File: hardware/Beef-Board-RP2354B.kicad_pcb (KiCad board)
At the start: 2 copper layers, 84 x 59.2 mm, 81 parts, among them J1 USB-C DEVICE, J10 VAUX OUT, J11 B1 LEGACY, J12 B2 LEGACY, J13 B3 LEGACY, J14 B4 LEGACY, J15 B5 LEGACY, J16 B6 LEGACY, J17 B7 LEGACY, J18 B8 LEGACY, J19 B9 LEGACY, J2 POWER SELECT, J20 B10 LEGACY, J21 B11 LEGACY, J22 USB COMMON, J3 VAUX 5V INPUT, J31 ENCODER 1, J32 ENCODER 2, J33 AE1 0-5V, J34 AE2 0-5V, J4 USB-C AUX POWER, J40 TT RGB, J41 CENTER BAR RGB, J42 UART A 3V3, J43 UART B 3V3, J5 ENC1 A, J6 ENC1 B, J60 RESET HEADER, J61 BOOTSEL HEADER, J7 ENC2 A, J8 ENC2 B, J9 VAUX OUT, Q1 2N7002, Q10 2N7002, Q11 2N7002, Q2 2N7002, Q3 2N7002, Q4 2N7002, Q5 2N7002, Q6 2N7002, Q7 2N7002, Q8 2N7002, Q9 2N7002, U1 RP2354B, U2 USBLC6-2SC6, U3 AP2112K-3.3, Y1 12MHz CL=10pF

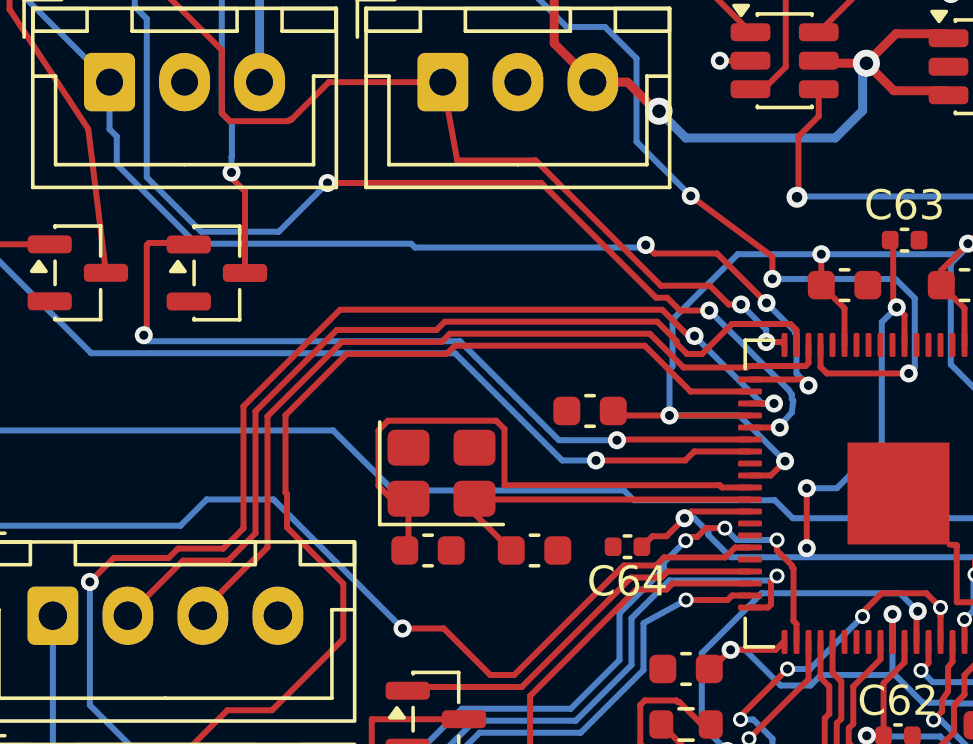
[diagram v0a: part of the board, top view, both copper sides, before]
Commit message: hardware: adopt corrected crystal routing and JLCPCB assembly settings
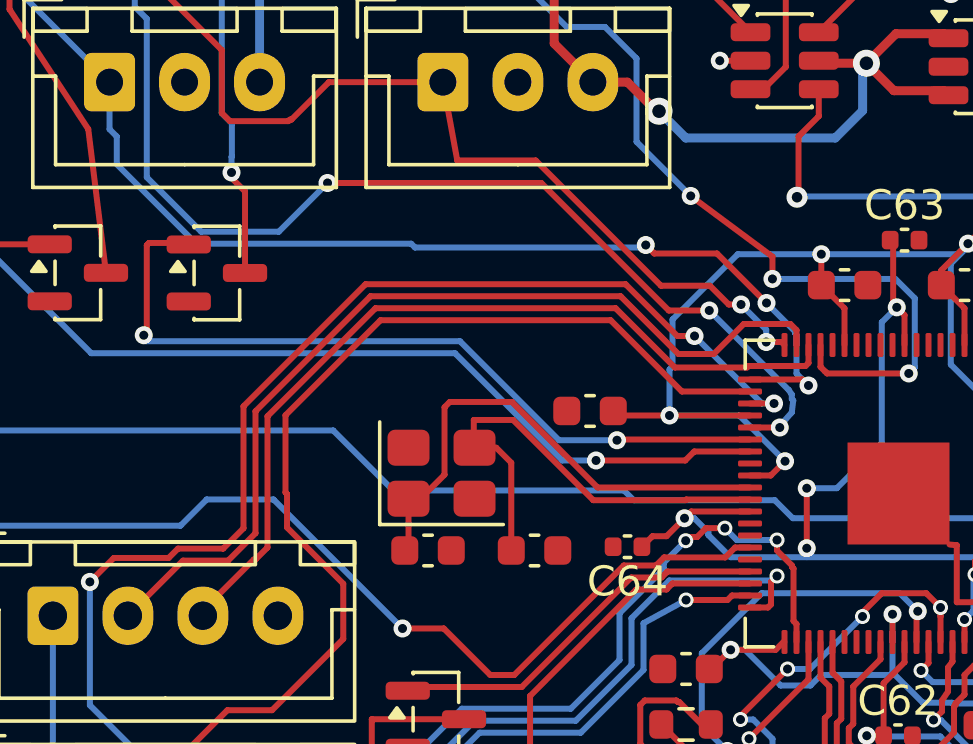
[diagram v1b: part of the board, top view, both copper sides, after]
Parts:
- J3: footprint TerminalBlock_Phoenix:TerminalBlock_Phoenix_MKDS-1,5-2_1x02_P5.00mm_Horizontal -> Connector_JST:JST_PH_B2B-PH-K_1x02_P2.00mm_Vertical
- J33, J34: footprint Connector_JST:JST_XH_B3B-XH-A_1x03_P2.50mm_Vertical -> Connector_JST:JST_PH_B3B-PH-K_1x03_P2.00mm_Vertical
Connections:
- Y1 pad 2: /HSE_OUT -> /GND
- Y1 pad 3: (no net) -> /HSE_OUT
- Y1 pad 4: (no net) -> /GND
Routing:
- net /HSE_OUT: track 10.7 -> 15.7 mm
- net /HSE_IN: track 18.6 -> 17.0 mm
- net /UART_B_TX_3V3: track 35.2 -> 35.9 mm
- net /UART_B_RX_3V3: track 40.5 -> 41.2 mm
- net /UART_A_TX_3V3: track 27.9 -> 28.6 mm
- net /UART_A_RX_3V3: track 30.7 -> 31.3 mm
